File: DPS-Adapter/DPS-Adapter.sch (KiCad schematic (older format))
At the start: 4 parts, among them J1 Conn_01x04, J2 Conn_01x04, J3 Conn_01x04, J4 Conn_01x04

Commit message: started with design of PCB Layout
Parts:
- J1, J2, J3, J4: footprint (none) -> Socket_Strips:Socket_Strip_Straight_1x04_Pitch2.54mm
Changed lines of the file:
@@
 LIBS:contrib
 LIBS:valves
+LIBS:DPS-Adapter-cache
 EELAYER 25 0
 EELAYER END
@@
 F 0 "J1" H 4000 2300 50  0000 C CNN
 F 1 "Conn_01x04" H 4000 1800 50  0000 C CNN
-F 2 "" H 4000 2100 50  0001 C CNN
+F 2 "Socket_Strips:Socket_Strip_Straight_1x04_Pitch2.54mm" H 4000 2100 50  0001 C CNN
 F 3 "" H 4000 2100 50  0001 C CNN
 	1    4000 2100
@@
 F 0 "J2" H 4000 3150 50  0000 C CNN
 F 1 "Conn_01x04" H 4000 2650 50  0000 C CNN
-F 2 "" H 4000 2950 50  0001 C CNN
+F 2 "Socket_Strips:Socket_Strip_Straight_1x04_Pitch2.54mm" H 4000 2950 50  0001 C CNN
 F 3 "" H 4000 2950 50  0001 C CNN
 	1    4000 2950
@@
 F 0 "J3" H 5400 2300 50  0000 C CNN
 F 1 "Conn_01x04" H 5400 1800 50  0000 C CNN
-F 2 "" H 5400 2100 50  0001 C CNN
+F 2 "Socket_Strips:Socket_Strip_Straight_1x04_Pitch2.54mm" H 5400 2100 50  0001 C CNN
 F 3 "" H 5400 2100 50  0001 C CNN
 	1    5400 2100
@@
 F 0 "J4" H 5400 3150 50  0000 C CNN
 F 1 "Conn_01x04" H 5400 2650 50  0000 C CNN
-F 2 "" H 5400 2950 50  0001 C CNN
+F 2 "Socket_Strips:Socket_Strip_Straight_1x04_Pitch2.54mm" H 5400 2950 50  0001 C CNN
 F 3 "" H 5400 2950 50  0001 C CNN
 	1    5400 2950

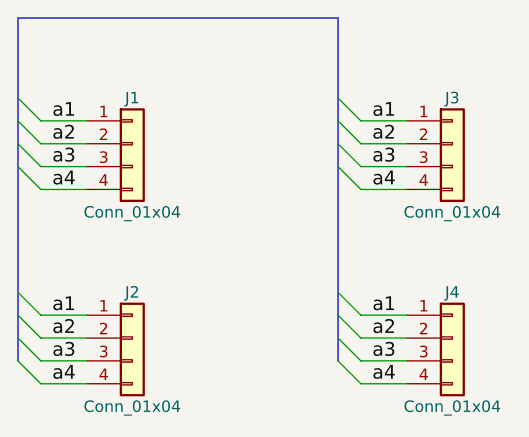
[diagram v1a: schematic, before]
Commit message: populate changes to archive correct version
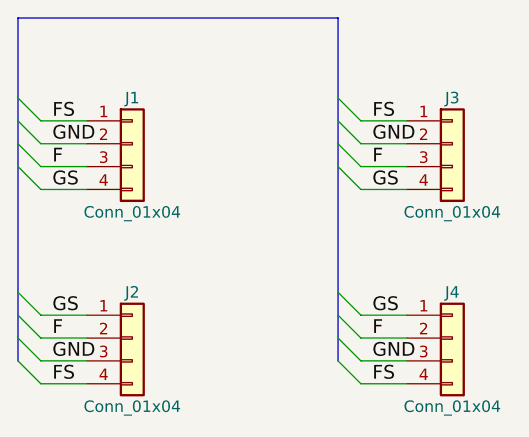
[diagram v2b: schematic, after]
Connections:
- net a1 renamed FS
- net FS: now also J2.4 (Pin_4), J4.4 (Pin_4); no longer J2.1 (Pin_1), J4.1 (Pin_1)
- net a2 renamed F
- net F: now also J1.3 (Pin_3), J3.3 (Pin_3); no longer J1.2 (Pin_2), J3.2 (Pin_2)
- net a3 renamed GND
- net GND: now also J1.2 (Pin_2), J3.2 (Pin_2); no longer J1.3 (Pin_3), J3.3 (Pin_3)
- net a4 renamed GS
- net GS: now also J2.1 (Pin_1), J4.1 (Pin_1); no longer J2.4 (Pin_4), J4.4 (Pin_4)
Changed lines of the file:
@@
 	5000 3150 5200 3150
 Text Label 3650 2000 0    60   ~ 0
-a1
+FS
 Text Label 3650 2100 0    60   ~ 0
-a2
+GND
 Text Label 3650 2200 0    60   ~ 0
-a3
+F
 Text Label 3650 2300 0    60   ~ 0
-a4
+GS
 Text Label 3650 2850 0    60   ~ 0
-a1
+GS
 Text Label 3650 2950 0    60   ~ 0
-a2
+F
 Text Label 3650 3050 0    60   ~ 0
-a3
+GND
 Text Label 3650 3150 0    60   ~ 0
-a4
+FS
 Text Label 5050 2000 0    60   ~ 0
-a1
+FS
 Text Label 5050 2100 0    60   ~ 0
-a2
+GND
 Text Label 5050 2200 0    60   ~ 0
-a3
+F
 Text Label 5050 2300 0    60   ~ 0
-a4
+GS
 Text Label 5050 2850 0    60   ~ 0
-a1
+GS
 Text Label 5050 2950 0    60   ~ 0
-a2
+F
 Text Label 5050 3050 0    60   ~ 0
-a3
+GND
 Text Label 5050 3150 0    60   ~ 0
-a4
+FS
 Wire Bus Line
 	3500 1550 3500 3050

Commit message: transition test to 5
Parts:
- J1, J2, J3, J4: symbol Conn_01x04 -> Connector_Generic:Conn_01x04
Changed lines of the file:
@@
-EESchema Schematic File Version 2
-LIBS:power
-LIBS:device
-LIBS:switches
-LIBS:relays
-LIBS:motors
-LIBS:transistors
-LIBS:conn
-LIBS:linear
-LIBS:regul
-LIBS:74xx
-LIBS:cmos4000
-LIBS:adc-dac
-LIBS:memory
-LIBS:xilinx
-LIBS:microcontrollers
-LIBS:dsp
-LIBS:microchip
-LIBS:analog_switches
-LIBS:motorola
-LIBS:texas
-LIBS:intel
-LIBS:audio
-LIBS:interface
-LIBS:digital-audio
-LIBS:philips
-LIBS:display
-LIBS:cypress
-LIBS:siliconi
-LIBS:opto
-LIBS:atmel
-LIBS:contrib
-LIBS:valves
+EESchema Schematic File Version 4
 LIBS:DPS-Adapter-cache
-EELAYER 25 0
+EELAYER 26 0
 EELAYER END
 $Descr A4 11693 8268
@@
 $EndDescr
 $Comp
-L Conn_01x04 J1
+L Connector_Generic:Conn_01x04 J1
 U 1 1 5AA59B04
 P 4000 2100
@@
 	3600 2300 3800 2300
 $Comp
-L Conn_01x04 J2
+L Connector_Generic:Conn_01x04 J2
 U 1 1 5AA59DDB
 P 4000 2950
@@
 	3600 3150 3800 3150
 $Comp
-L Conn_01x04 J3
+L Connector_Generic:Conn_01x04 J3
 U 1 1 5AA59E14
 P 5400 2100
@@
 	5000 2300 5200 2300
 $Comp
-L Conn_01x04 J4
+L Connector_Generic:Conn_01x04 J4
 U 1 1 5AA59E88
 P 5400 2950
@@
 FS
 Wire Bus Line
-	3500 1550 3500 3050
-Wire Bus Line
 	3500 1550 4900 1550
-Wire Bus Line
-	4900 1550 4900 3050
 Entry Wire Line
 	3500 1900 3600 2000
@@
 Entry Wire Line
 	4900 3050 5000 3150
+Wire Bus Line
+	3500 1550 3500 3050
+Wire Bus Line
+	4900 1550 4900 3050
 $EndSCHEMATC
